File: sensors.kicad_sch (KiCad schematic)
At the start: 44 parts, among them Q2 IRLML6402, Q801 IRLML6402, Q802 IRLML6402, Q803 IRLML6402, Q804 IRLML6402, Q805 IRLML6402, U801 TPS61023DRLR, U802 ISL83078EIBZA, X12 Conn_01x04_Pin, X13 Conn_01x07_Pin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

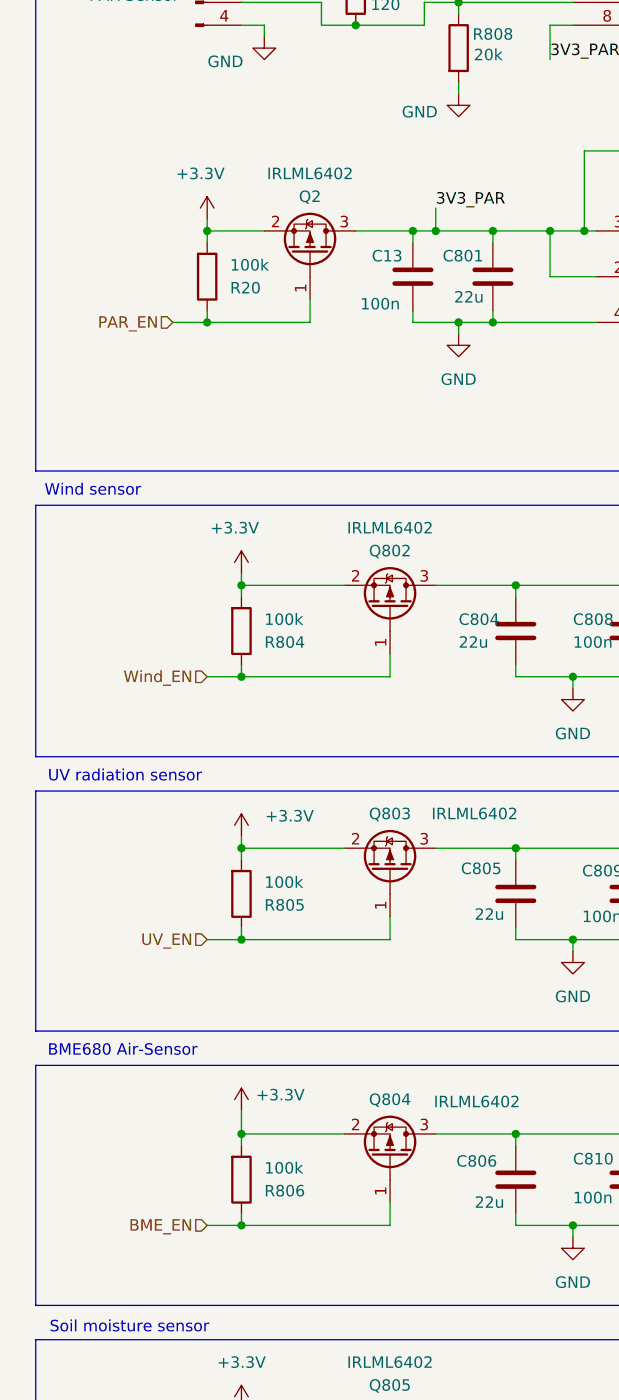
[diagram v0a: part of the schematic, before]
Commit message: Add SamacSys & CAPPRD library; update KiCad
Add a new SamacSys parts library and a complete CAPPRD500 footprint/package set (870585375004) with multi-EDA exports and 3D STEP models. Also add sym-lib-table and SamacSys parts entries, and update KiCad project files (schematics, PCB, project file and generated PDFs) to reference the new parts and footprints.
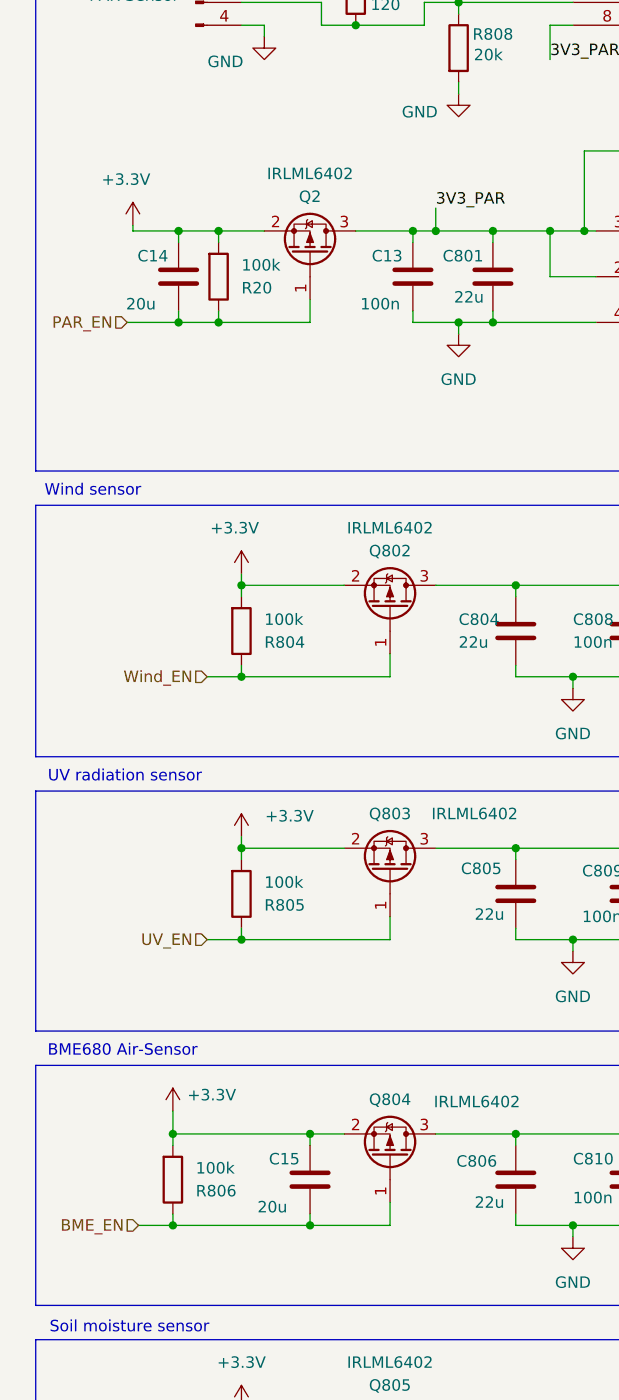
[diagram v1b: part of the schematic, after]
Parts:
- added C14, C15: 20u, Capacitor_SMD:C_0805_2012Metric_Pad1.18x1.45mm_HandSolder, symbol Device:C
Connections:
- net +3.3V: now also C14.2, C15.2
- net BME_EN: now also C15.1
- net PAR_EN: now also C14.1
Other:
- moved on the sheet: R20, R806
